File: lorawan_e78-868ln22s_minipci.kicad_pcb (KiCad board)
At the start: 2 copper layers, 30 x 51 mm, 7 parts, among them Con1 MiniPci, P1 RF2-03E-T-00-50-G, U8 IP4220CZ6

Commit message: Finalized project
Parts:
- added C3: 100n_50V, Capacitors_Smd_0603:100nF_0603, F.Cu at (162.8, 82.0)
- added C4: 100n_50V, Capacitors_Smd_0603:100nF_0603, F.Cu at (143.3, 104.7)
- added Con2: TC2050-IDC-NL, Tag_Connectors:TC2050-IDC-NL, F.Cu at (145.0, 84.8)
- added NTC1: NTCS0603E3103FMT, NTC_Thermistors:NTCS0603E3103FMT, F.Cu at (148.3, 97.5)
- added R2: 4k7, Resistor_Smd_0603:4k7_0603, F.Cu at (143.7, 95.0)
- added R3: 4k7, Resistor_Smd_0603:4k7_0603, F.Cu at (145.1, 95.0)
- added R4: 4k7, Resistor_Smd_0603:4k7_0603, F.Cu at (148.2, 95.2)
- added R5: 4k7, Resistor_Smd_0603:4k7_0603, F.Cu at (158.0, 85.6)
- added R6: 0R, Resistor_Smd_0603:0R_0603, F.Cu at (148.5, 81.2)
- added R7: 0R, Resistor_Smd_0603:0R_0603, F.Cu at (157.8, 77.1)
- added R8: 0R, Resistor_Smd_0603:0R_0603, F.Cu at (155.3, 77.1)
- added U1: DS18B20U, Temperature_Sensors:DS18B20U_MSOP-8_3x3mm_P0.65mm, F.Cu at (162.8, 84.6)
- added U2: TCN75A, Temperature_Sensors:TCN75A_SOIC8, F.Cu at (143.1, 100.0)
- moved U8 16.0 mm to (157.1, 80.7), turned to 0 degrees
- moved C2 10.6 mm to (149.7, 90.7), turned to 90 degrees
- moved C1 7.83 mm to (148.2, 90.7), turned to 90 degrees
- moved R1 4.79 mm to (148.6, 92.8), turned to 180 degrees
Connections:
- Con1 pad 11: (no net) -> Net-(Con1-Pad11)
- Con1 pad 13: (no net) -> Net-(Con1-Pad13)
- Con1 pad 17: Net-(Con1-Pad17) -> (no net)
- Con1 pad 19: Net-(Con1-Pad19) -> (no net)
- Con1 pad 22: Net-(C1-Pad1) -> Net-(Con1-Pad22)
- Module1 pad 17: (no net) -> Net-(Module1-Pad17)
- Module1 pad 20: Net-(Con1-Pad19) -> Net-(Con1-Pad11)
- Module1 pad 21: Net-(Con1-Pad17) -> Net-(Con1-Pad13)
- Module1 pad 22: Net-(Con1-Pad10) -> Net-(Con2-Pad10)
- Module1 pad 23: Net-(Con1-Pad12) -> Net-(Con2-Pad6)
- Module1 pad 4: (no net) -> Net-(Module1-Pad4)
- Module1 pad 6: (no net) -> Net-(Module1-Pad6)
- Module1 pad 7: (no net) -> Net-(Module1-Pad7)
- U8 pad 1: Net-(Con1-Pad19) -> Net-(Con1-Pad11)
- U8 pad 3: Net-(Con1-Pad17) -> Net-(Con1-Pad13)
- U8 pad 4: Net-(Con1-Pad10) -> Net-(Con2-Pad10)
- U8 pad 6: Net-(Con1-Pad12) -> Net-(Con2-Pad6)
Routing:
- net 3V3: track 0.00 -> 119.2 mm, vias 0 -> 4
- net GND: track 0.00 -> 100.9 mm, vias 0 -> 52
- net Net-(C1-Pad1): track 0.00 -> 47.5 mm, vias 0 -> 4
- net Net-(Con2-Pad10): track 0.00 -> 46.5 mm, vias 0 -> 3
- net Net-(Con2-Pad6): track 0.00 -> 41.1 mm, vias 0 -> 2
- net Net-(Con1-Pad11): track 0.00 -> 34.6 mm, vias 0 -> 3
- net Net-(Module1-Pad17): track 0.00 -> 33.3 mm, vias 0 -> 3
- net Net-(Con1-Pad13): track 0.00 -> 31.8 mm, vias 0 -> 3
- net Net-(Module1-Pad4): track 0.00 -> 28.9 mm, vias 0 -> 2
- net Net-(Con1-Pad20): track 0.00 -> 28.5 mm, vias 0 -> 1
- net Net-(Con1-Pad22): track 0.00 -> 12.5 mm, vias 0 -> 1
- net Net-(Module1-Pad7): track 0.00 -> 11.1 mm
- net Net-(Module1-Pad6): track 0.00 -> 9.99 mm
- net Net-(Module1-Pad11): track 0.00 -> 9.62 mm
- net Net-(Con1-Pad12): track 0.00 -> 8.77 mm, vias 0 -> 1
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
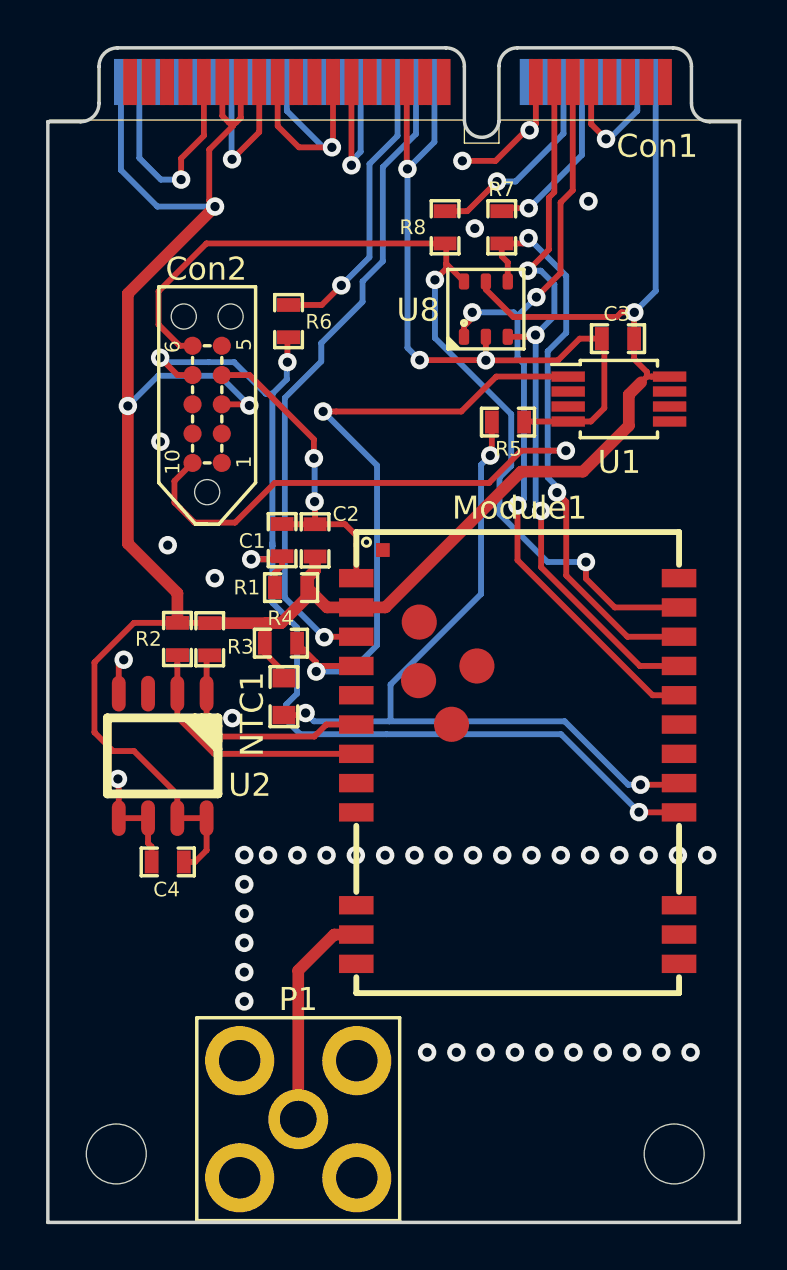
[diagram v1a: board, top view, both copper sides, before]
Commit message: Added some pcb description
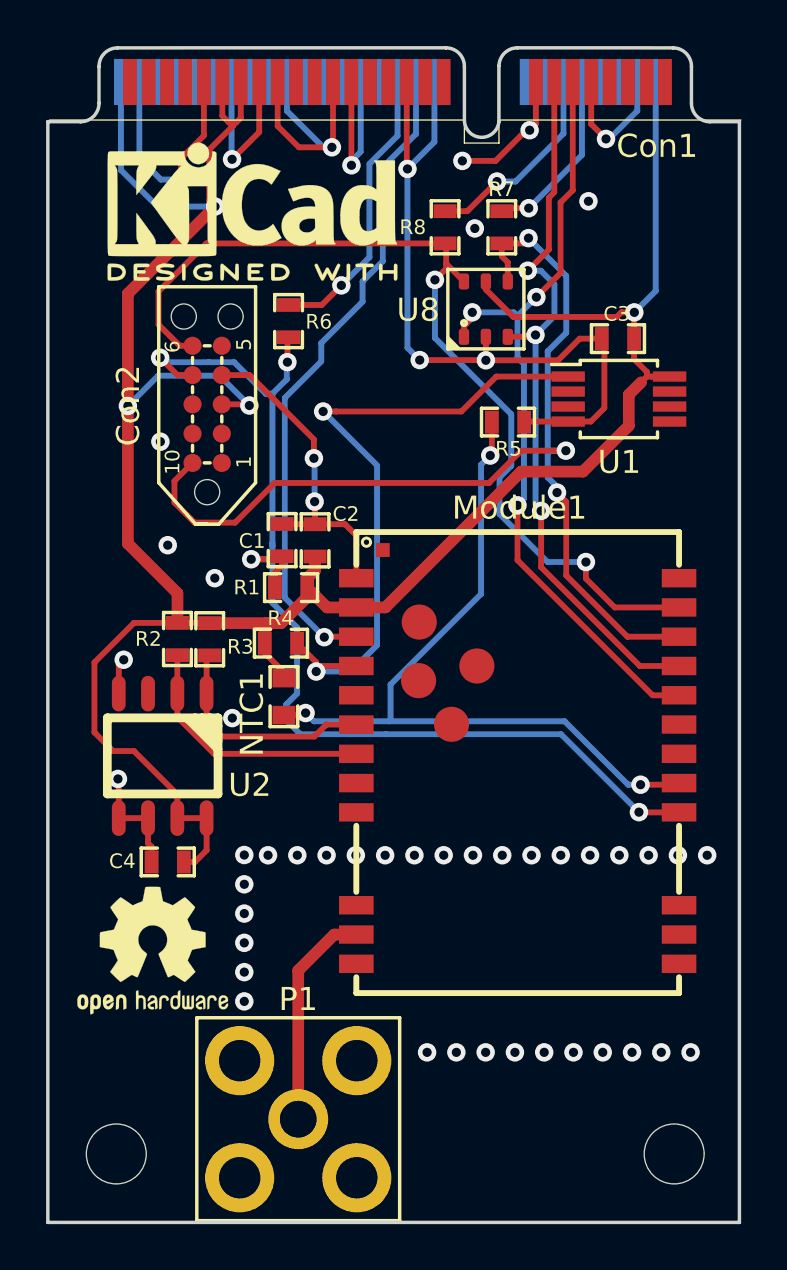
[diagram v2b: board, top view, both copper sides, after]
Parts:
- added REF**: KiCad-Logo2_5mm_SilkScreen, Symbols:KiCad-Logo2_5mm_SilkScreen, F.Cu at (146.9, 76.4)
- added REFe: OSHW-Logo2_7.3x6mm_SilkScreen, Symbols:OSHW-Logo2_7.3x6mm_SilkScreen, F.Cu at (142.6, 108.5)
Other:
- net class Default removed

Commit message: Modified Lora module footprint
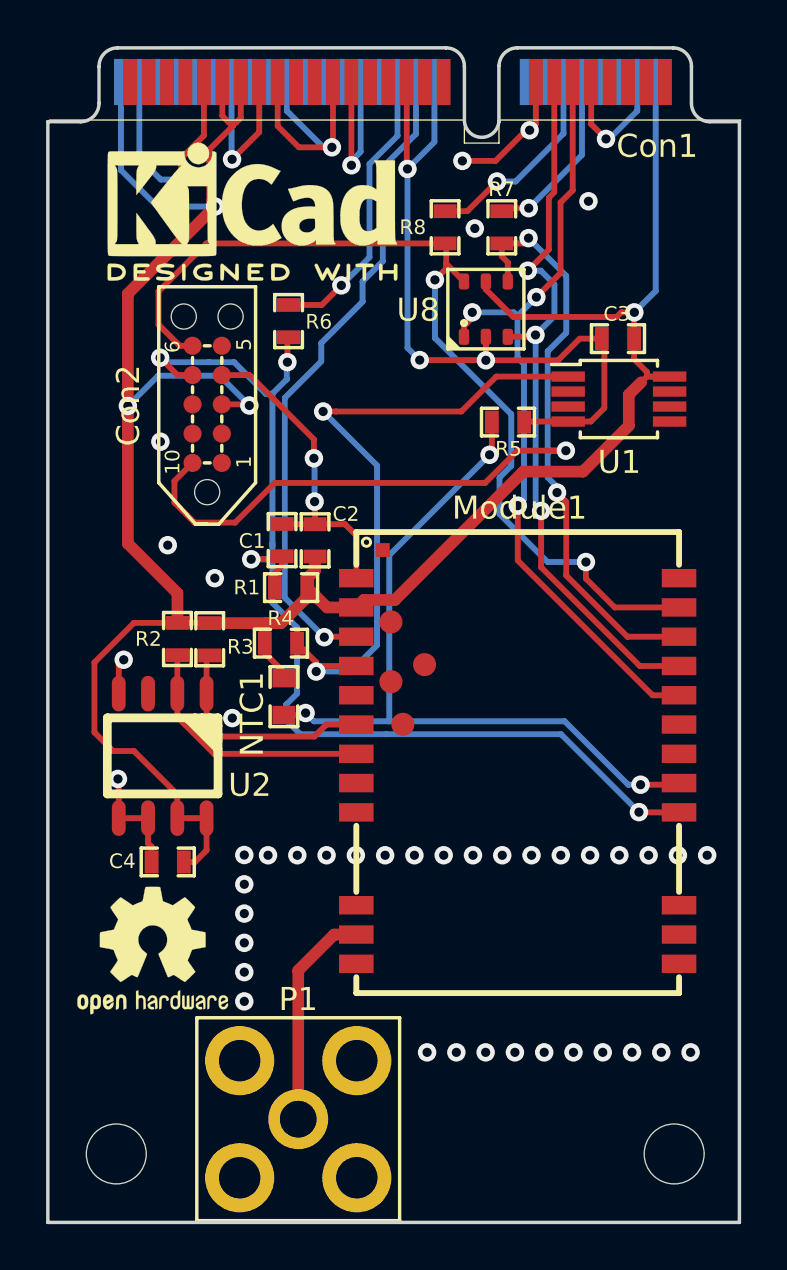
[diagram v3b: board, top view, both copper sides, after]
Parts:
- Module1: value E78-868LN22S -> REF?

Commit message: Corrected project
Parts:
- removed Con2: TC2050-IDC-NL, Tag_Connectors:TC2050-IDC-NL
- removed R7, R8: 0R, Resistor_Smd_0603:0R_0603
- removed U8: IP4220CZ6, ESD_Protectors:IP4220CZ6_SOT457
- added REF**: KiCad-Logo2_8mm_SilkScreen, Symbols:KiCad-Logo2_8mm_SilkScreen, B.Cu at (152.7, 93.3)
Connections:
- Con1 pad 10: Net-(Con1-Pad10) -> (no net)
- Con1 pad 11: Net-(Con1-Pad11) -> (no net)
- Con1 pad 12: Net-(Con1-Pad12) -> (no net)
- Con1 pad 13: Net-(Con1-Pad13) -> (no net)
- Con1 pad 17: (no net) -> Net-(Con1-Pad17)
- Con1 pad 19: (no net) -> Net-(Con1-Pad19)
- Con1 pad 30: (no net) -> Net-(Con1-Pad30)
- Con1 pad 32: (no net) -> Net-(Con1-Pad32)
- Con1 pad 45: (no net) -> Net-(Con1-Pad45)
- Con1 pad 51: (no net) -> Net-(Con1-Pad51)
- Module1 pad 17: Net-(Module1-Pad17) -> (no net)
- Module1 pad 20: Net-(Con1-Pad11) -> Net-(Con1-Pad17)
- Module1 pad 21: Net-(Con1-Pad13) -> Net-(Con1-Pad19)
- Module1 pad 22: Net-(Con2-Pad10) -> (no net)
- Module1 pad 23: Net-(Con2-Pad6) -> (no net)
- Module1 pad 4: Net-(Module1-Pad4) -> (no net)
- Module1 pad 6: Net-(Module1-Pad6) -> (no net)
- Module1 pad 7: Net-(Module1-Pad7) -> (no net)
- NTC1 pad 1: Net-(Module1-Pad17) -> Net-(Con1-Pad51)
- R2 pad 2: Net-(Module1-Pad7) -> Net-(Con1-Pad30)
- R3 pad 2: Net-(Module1-Pad6) -> Net-(Con1-Pad32)
- R4 pad 2: Net-(Module1-Pad4) -> Net-(Con1-Pad45)
- R5 pad 1: Net-(Module1-Pad17) -> Net-(Con1-Pad51)
- U1 pad 1: Net-(Module1-Pad4) -> Net-(Con1-Pad45)
- U2 pad 1: Net-(Module1-Pad6) -> Net-(Con1-Pad32)
- U2 pad 2: Net-(Module1-Pad7) -> Net-(Con1-Pad30)
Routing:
- net Net-(Con1-Pad45): track 0.00 -> 46.7 mm, vias 0 -> 4
- net Net-(Con2-Pad10): track 46.5 -> 0.00 mm, vias 3 -> 0
- net Net-(Con1-Pad51): track 0.00 -> 45.1 mm, vias 0 -> 4
- net Net-(Con2-Pad6): track 41.1 -> 0.00 mm, vias 2 -> 0
- net Net-(Con1-Pad11): track 34.6 -> 0.00 mm, vias 3 -> 0
- net Net-(Module1-Pad17): track 33.3 -> 0.00 mm, vias 3 -> 0
- net Net-(Con1-Pad30): track 0.00 -> 32.5 mm, vias 0 -> 1
- net Net-(Con1-Pad13): track 31.8 -> 0.00 mm, vias 3 -> 0
- net Net-(Con1-Pad17): track 0.00 -> 31.5 mm, vias 0 -> 2
- net Net-(Con1-Pad32): track 0.00 -> 31.4 mm, vias 0 -> 1
- net Net-(Con1-Pad19): track 0.00 -> 30.9 mm, vias 0 -> 2
- net GND: track 100.9 -> 71.6 mm, vias 52 -> 72
- net Net-(Module1-Pad4): track 28.9 -> 0.00 mm, vias 2 -> 0
- net 3V3: track 119.2 -> 102.7 mm, vias 4 -> 2
- net Net-(Module1-Pad7): track 11.1 -> 0.00 mm
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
